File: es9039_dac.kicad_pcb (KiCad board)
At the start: 2 copper layers, 68.5 x 67.4 mm, 24 parts, among them J1 Conn_02x07_Odd_Even, U1 ES9039Q2M, U2 TPS7A2033DBV, U3 TPS7A2033DBV

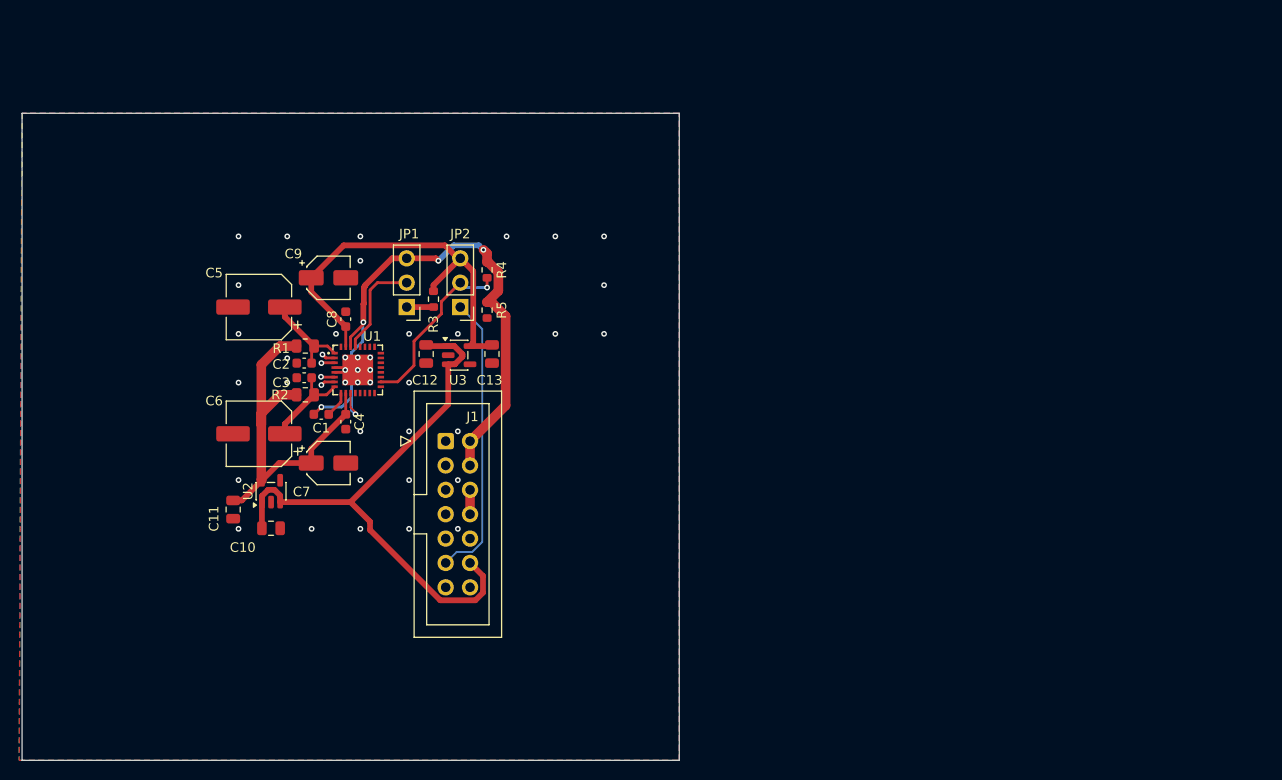
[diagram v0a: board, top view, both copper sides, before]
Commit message: deleted pcb and some changes in schematic
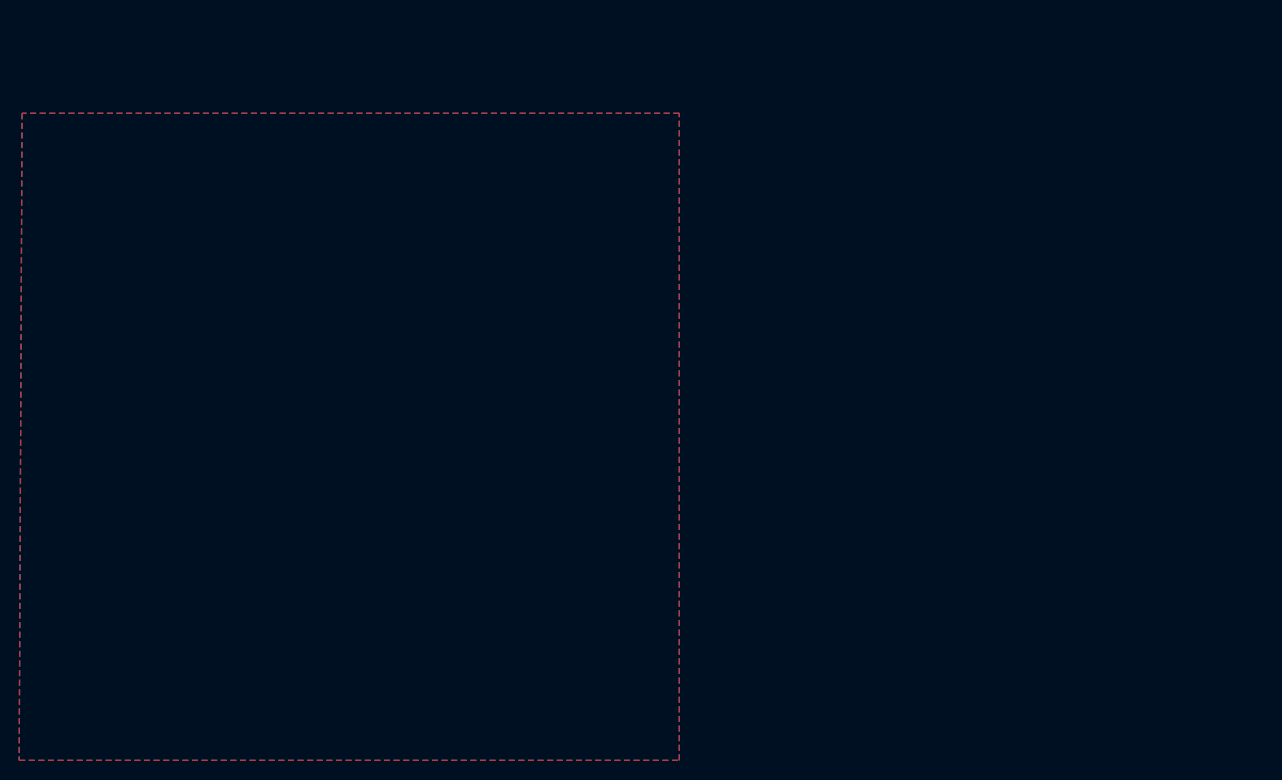
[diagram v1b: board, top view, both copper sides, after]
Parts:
- removed C1, C2, C3, C4, C8: 100n, Capacitor_SMD:C_0603_1608Metric
- removed C10, C11, C12, C13: 4u7, Capacitor_SMD:C_0805_2012Metric
- removed C5, C6: 100u, Capacitor_SMD:CP_Elec_6.3x5.8
- removed C7, C9: 10u, Capacitor_SMD:CP_Elec_4x5.4
- removed J1: Conn_02x07_Odd_Even, Connector_IDC:IDC-Header_2x07_P2.54mm_Vertical
- removed JP1: DAC_MODE1, Connector_PinHeader_2.54mm:PinHeader_1x03_P2.54mm_Vertical
- removed JP2: DAC_MODE2, Connector_PinHeader_2.54mm:PinHeader_1x03_P2.54mm_Vertical
- removed R1, R2: 2.2R, Resistor_SMD:R_0805_2012Metric
- removed R3: 10K, Resistor_SMD:R_0603_1608Metric
- removed R4: 100K, Resistor_SMD:R_0603_1608Metric
- removed R5: 0, Resistor_SMD:R_0603_1608Metric
- removed U1: ES9039Q2M, EasyEDA:QFN-32_L5.0-W5.0-P0.50-TL-EP3.2
- removed U2, U3: TPS7A2033DBV, Package_TO_SOT_SMD:SOT-23-5
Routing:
- net GNDD: track 65.2 -> 0.00 mm, vias 5 -> 0
- net +5V: track 61.2 -> 0.00 mm
- net +3.3V: track 42.7 -> 0.00 mm
- net +3.3VA: track 40.7 -> 0.00 mm
- net /STBY: track 30.4 -> 0.00 mm
- net Net-(JP2-C): track 18.8 -> 0.00 mm, vias 1 -> 0
- net /MODE: track 10.7 -> 0.00 mm
- net Net-(U1-AVCC_DAC2): track 9.70 -> 0.00 mm
- net Net-(U1-AVCC_DAC1): track 9.66 -> 0.00 mm
- net GNDA: track 7.57 -> 0.00 mm, vias 40 -> 0
- net Net-(JP1-A): track 2.79 -> 0.00 mm
- net Net-(U1-DVDD): track 2.74 -> 0.00 mm
- net unconnected-(U1-DAC2-Pad7): track 1.51 -> 0.00 mm, vias 1 -> 0
- net unconnected-(U1-DAC2B-Pad6): track 1.44 -> 0.00 mm, vias 1 -> 0
- net unconnected-(U1-DAC1B-Pad2): track 1.41 -> 0.00 mm, vias 1 -> 0
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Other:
- board outline removed
- copper layers 2 -> 4

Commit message: trace dac chip and add output stage
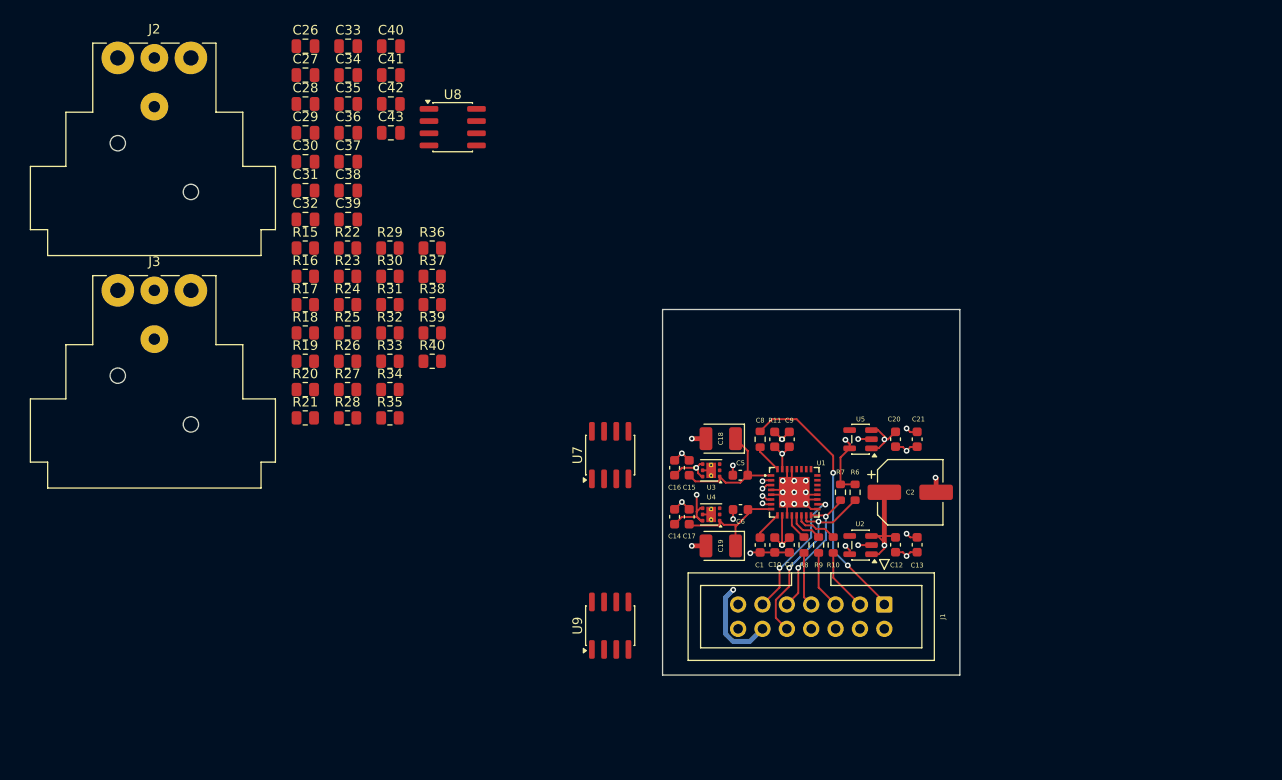
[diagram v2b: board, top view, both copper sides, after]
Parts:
- added C1: 100n, Capacitor_SMD:C_0603_1608Metric, F.Cu at (216.9, 100.7)
- added C10: 10u, Capacitor_SMD:C_0603_1608Metric, F.Cu at (218.4, 100.7)
- added C12: 4u7, Capacitor_SMD:C_0603_1608Metric, F.Cu at (231.0, 100.7)
- added C13: 4u7, Capacitor_SMD:C_0603_1608Metric, F.Cu at (233.3, 100.7)
- added C14: 1u, Capacitor_SMD:C_0603_1608Metric, F.Cu at (208.0, 97.8)
- added C15: 1u, Capacitor_SMD:C_0603_1608Metric, F.Cu at (209.5, 92.7)
- added C16: 1u, Capacitor_SMD:C_0603_1608Metric, F.Cu at (208.0, 92.7)
- added C17: 1u, Capacitor_SMD:C_0603_1608Metric, F.Cu at (209.5, 97.8)
- added C18: 47u, Capacitor_Tantalum_SMD:CP_EIA-3528-12_Kemet-T, F.Cu at (212.8, 89.7)
- added C19: 47u, Capacitor_Tantalum_SMD:CP_EIA-3528-12_Kemet-T, F.Cu at (212.8, 100.8)
- added C2: 100u, Capacitor_SMD:CP_Elec_6.3x5.8, F.Cu at (232.6, 95.2)
- added C20: 4u7, Capacitor_SMD:C_0603_1608Metric, F.Cu at (231.0, 89.7)
- added C21: 4u7, Capacitor_SMD:C_0603_1608Metric, F.Cu at (233.3, 89.7)
- added C26: 510p, Capacitor_SMD:C_0805_2012Metric, F.Cu at (169.5, 48.8)
- added C27: 510p, Capacitor_SMD:C_0805_2012Metric, F.Cu at (169.5, 51.8)
- added C28: 51p, Capacitor_SMD:C_0805_2012Metric, F.Cu at (169.5, 54.8)
- added C29: 2n2, Capacitor_SMD:C_0805_2012Metric, F.Cu at (169.5, 57.8)
- added C30: 2n2, Capacitor_SMD:C_0805_2012Metric, F.Cu at (169.5, 60.8)
- added C31: 470n, Capacitor_SMD:C_0805_2012Metric, F.Cu at (169.5, 63.8)
- added C32: 470n, Capacitor_SMD:C_0805_2012Metric, F.Cu at (169.5, 66.8)
- added C33: 2n2, Capacitor_SMD:C_0805_2012Metric, F.Cu at (174.0, 48.8)
- added C34: 2n2, Capacitor_SMD:C_0805_2012Metric, F.Cu at (174.0, 51.8)
- added C35: 510p, Capacitor_SMD:C_0805_2012Metric, F.Cu at (174.0, 54.8)
- added C36: 510p, Capacitor_SMD:C_0805_2012Metric, F.Cu at (174.0, 57.8)
- added C37: 51p, Capacitor_SMD:C_0805_2012Metric, F.Cu at (174.0, 60.8)
- added C38: 2n2, Capacitor_SMD:C_0805_2012Metric, F.Cu at (174.0, 63.8)
- added C39: 2n2, Capacitor_SMD:C_0805_2012Metric, F.Cu at (174.0, 66.8)
- added C4: 100n, Capacitor_SMD:C_0603_1608Metric, F.Cu at (220.0, 100.7)
- added C40: 470n, Capacitor_SMD:C_0805_2012Metric, F.Cu at (178.4, 48.8)
- added C41: 470n, Capacitor_SMD:C_0805_2012Metric, F.Cu at (178.4, 51.8)
- added C42: 470n, Capacitor_SMD:C_0805_2012Metric, F.Cu at (178.4, 54.8)
- added C43: 470n, Capacitor_SMD:C_0805_2012Metric, F.Cu at (178.4, 57.8)
- added C5: 100n, Capacitor_SMD:C_0603_1608Metric, F.Cu at (214.9, 93.5)
- added C6: 100n, Capacitor_SMD:C_0603_1608Metric, F.Cu at (214.9, 97.1)
- added C8: 100n, Capacitor_SMD:C_0603_1608Metric, F.Cu at (218.4, 89.7)
- added C9: 4u7, Capacitor_SMD:C_0603_1608Metric, F.Cu at (220.0, 89.7)
- added J1: Conn_02x07_Odd_Even, Connector_IDC:IDC-Header_2x07_P2.54mm_Vertical, F.Cu at (229.9, 106.9)
- added J2: XLR3, Connector_Audio:Jack_XLR_Neutrik_NC3MAH_Horizontal, F.Cu at (150.0, 50.0)
- added J3: XLR3, Connector_Audio:Jack_XLR_Neutrik_NC3MAH_Horizontal, F.Cu at (150.0, 74.2)
- added R10: 22R, Resistor_SMD:R_0603_1608Metric, F.Cu at (224.5, 100.7)
- added R11: 22R, Resistor_SMD:R_0603_1608Metric, F.Cu at (216.9, 89.7)
- added R15: 1K8, Resistor_SMD:R_0805_2012Metric, F.Cu at (169.5, 69.8)
- added R16: 1K8, Resistor_SMD:R_0805_2012Metric, F.Cu at (169.5, 72.7)
- added R17: 1K8, Resistor_SMD:R_0805_2012Metric, F.Cu at (169.5, 75.7)
- added R18: 1K8, Resistor_SMD:R_0805_2012Metric, F.Cu at (169.5, 78.6)
- added R19: 3K2, Resistor_SMD:R_0805_2012Metric, F.Cu at (169.5, 81.6)
- added R20: 3K2, Resistor_SMD:R_0805_2012Metric, F.Cu at (169.5, 84.5)
- added R21: 4R3, Resistor_SMD:R_0805_2012Metric, F.Cu at (169.5, 87.5)
- added R22: 4R3, Resistor_SMD:R_0805_2012Metric, F.Cu at (173.9, 69.8)
- added R23: 1M2, Resistor_SMD:R_0805_2012Metric, F.Cu at (173.9, 72.7)
- added R24: 10K, Resistor_SMD:R_0805_2012Metric, F.Cu at (173.9, 75.7)
- added R25: 10K, Resistor_SMD:R_0805_2012Metric, F.Cu at (173.9, 78.6)
- added R26: 140, Resistor_SMD:R_0805_2012Metric, F.Cu at (173.9, 81.6)
- added R27: 140, Resistor_SMD:R_0805_2012Metric, F.Cu at (173.9, 84.5)
- added R28: 4R3, Resistor_SMD:R_0805_2012Metric, F.Cu at (173.9, 87.5)
- added R29: 4R3, Resistor_SMD:R_0805_2012Metric, F.Cu at (178.3, 69.8)
- added R30: 1K8, Resistor_SMD:R_0805_2012Metric, F.Cu at (178.3, 72.7)
- added R31: 1K8, Resistor_SMD:R_0805_2012Metric, F.Cu at (178.3, 75.7)
- added R32: 1K8, Resistor_SMD:R_0805_2012Metric, F.Cu at (178.3, 78.6)
- added R33: 1K8, Resistor_SMD:R_0805_2012Metric, F.Cu at (178.3, 81.6)
- added R34: 3K2, Resistor_SMD:R_0805_2012Metric, F.Cu at (178.3, 84.5)
- added R35: 3K2, Resistor_SMD:R_0805_2012Metric, F.Cu at (178.3, 87.5)
- added R36: 1M2, Resistor_SMD:R_0805_2012Metric, F.Cu at (182.7, 69.8)
- added R37: 10K, Resistor_SMD:R_0805_2012Metric, F.Cu at (182.7, 72.7)
- added R38: 10K, Resistor_SMD:R_0805_2012Metric, F.Cu at (182.7, 75.7)
- added R39: 140, Resistor_SMD:R_0805_2012Metric, F.Cu at (182.7, 78.6)
- added R40: 140, Resistor_SMD:R_0805_2012Metric, F.Cu at (182.7, 81.6)
- added R6: 10K, Resistor_SMD:R_0603_1608Metric, F.Cu at (226.8, 95.2)
- added R7: 10K, Resistor_SMD:R_0603_1608Metric, F.Cu at (225.3, 95.2)
- added R8: 22R, Resistor_SMD:R_0603_1608Metric, F.Cu at (221.5, 100.7)
- added R9: 22R, Resistor_SMD:R_0603_1608Metric, F.Cu at (223.0, 100.7)
- added U1: ES9039Q2M, EasyEDA:QFN-32_L5.0-W5.0-P0.50-TL-EP3.2, F.Cu at (220.5, 95.2)
- added U2: TPS7A2033DBV, Package_TO_SOT_SMD:SOT-23-5, F.Cu at (227.4, 100.8)
- added U3: LP5912-3.3DRV, Package_SON:WSON-6-1EP_2x2mm_P0.65mm_EP1x1.6mm_ThermalVias, F.Cu at (211.8, 93.0)
- added U4: LP5912-3.3DRV, Package_SON:WSON-6-1EP_2x2mm_P0.65mm_EP1x1.6mm_ThermalVias, F.Cu at (211.8, 97.6)
- added U5: TPS7A2033DBV, Package_TO_SOT_SMD:SOT-23-5, F.Cu at (227.4, 89.7)
- added U7: OPA1612AxD, Package_SO:SOIC-8_3.9x4.9mm_P1.27mm, F.Cu at (201.3, 91.4)
- added U8: OPA1612AxD, Package_SO:SOIC-8_3.9x4.9mm_P1.27mm, F.Cu at (184.9, 57.2)
- added U9: OPA1612AxD, Package_SO:SOIC-8_3.9x4.9mm_P1.27mm, F.Cu at (201.3, 109.2)
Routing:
- net +5V: track 0.00 -> 81.9 mm, vias 0 -> 5
- net GNDA: track 0.00 -> 48.4 mm, vias 0 -> 22
- net /es9039_dac/I2S_MCLK: track 0.00 -> 27.4 mm, vias 0 -> 2
- net +3.3V: track 0.00 -> 25.9 mm, vias 0 -> 3
- net +3.3VA: track 0.00 -> 21.7 mm, vias 0 -> 3
- net /es9039_dac/I2C_SCL: track 0.00 -> 20.2 mm, vias 0 -> 2
- net /es9039_dac/I2C_SDA: track 0.00 -> 14.8 mm, vias 0 -> 2
- net /es9039_dac/DAC_STBY: track 0.00 -> 14.4 mm, vias 0 -> 2
- net +3.3VAL: track 0.00 -> 13.9 mm
- net +3.3VAR: track 0.00 -> 12.1 mm
- net /es9039_dac/I2S_DATA: track 0.00 -> 6.53 mm
- net /es9039_dac/I2S_LRCK: track 0.00 -> 6.12 mm
- net /es9039_dac/I2S_BCLK: track 0.00 -> 5.69 mm
- net Net-(U1-DATA2): track 0.00 -> 4.62 mm
- net Net-(U1-DATA1): track 0.00 -> 3.75 mm
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- added copper zone on In1.Cu, net GNDA
- removed copper zone on B.Cu, net GNDA
- removed copper zone on F.Cu, net GNDA
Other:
- board outline added: 31 x 38.1 mm

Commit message: traced o/s
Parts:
- added C44: 470n, Capacitor_SMD:C_0805_2012Metric, F.Cu at (263.9, 71.7)
- added C45: 470n, Capacitor_SMD:C_0805_2012Metric, F.Cu at (263.9, 74.7)
- added R1: 10K, Resistor_SMD:R_0805_2012Metric, F.Cu at (255.1, 65.1)
- added R12: 10K, Resistor_SMD:R_0805_2012Metric, F.Cu at (259.5, 65.1)
- added R13: 10K, Resistor_SMD:R_0805_2012Metric, F.Cu at (259.5, 68.1)
- added R14: 10K, Resistor_SMD:R_0805_2012Metric, F.Cu at (259.5, 71.0)
- added R2: 10K, Resistor_SMD:R_0805_2012Metric, F.Cu at (255.1, 68.1)
- added R3: 100R, Resistor_SMD:R_0805_2012Metric, F.Cu at (255.1, 71.0)
- added R4: 10K, Resistor_SMD:R_0805_2012Metric, F.Cu at (255.1, 74.0)
- added R41: 10K, Resistor_SMD:R_0805_2012Metric, F.Cu at (259.5, 74.0)
- added R42: 100R, Resistor_SMD:R_0805_2012Metric, F.Cu at (259.5, 76.9)
- added R5: 10K, Resistor_SMD:R_0805_2012Metric, F.Cu at (255.1, 76.9)
- added U6: OPA1612AxD, Package_SO:SOIC-8_3.9x4.9mm_P1.27mm, F.Cu at (265.9, 67.0)
- J2: value XLR3 -> XLR_L; footprint Connector_Audio:Jack_XLR_Neutrik_NC3MAH_Horizontal -> Connector_Audio:Jack_XLR_Neutrik_NC3MAH-0_Horizontal
- J3: value XLR3 -> XLR_R; footprint Connector_Audio:Jack_XLR_Neutrik_NC3MAH_Horizontal -> Connector_Audio:Jack_XLR_Neutrik_NC3MAH-0_Horizontal
- moved C34 64.7 mm to (208.3, 106.7), turned to 90 degrees
- moved J2 64.6 mm to (213.4, 62.2)
- moved C35 61.4 mm to (196.8, 111.8), turned to -90 degrees
- moved C31 59.2 mm to (199.4, 114.9), turned to 180 degrees
- moved C32 58.7 mm to (203.2, 114.9)
- moved C28 55.4 mm to (204.5, 97.8), turned to -90 degrees
- moved C36 54.0 mm to (196.8, 106.7), turned to 90 degrees
- moved C26 52.8 mm to (196.8, 94.0), turned to -90 degrees
- moved C33 52.8 mm to (208.3, 88.9), turned to 90 degrees
- moved C37 52.0 mm to (204.5, 102.9), turned to 90 degrees
- moved C38 49.0 mm to (184.2, 111.8), turned to -90 degrees
- moved C42 48.8 mm to (186.7, 102.9), turned to -90 degrees
- moved C27 46.1 mm to (196.8, 88.9), turned to 90 degrees
- moved R29 45.9 mm to (205.7, 106.7), turned to -90 degrees
- moved U8 43.7 mm to (191.8, 100.3), turned to -90 degrees
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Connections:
- net Net-(C29-Pad1) renamed OUT_L
- net Net-(C30-Pad1) renamed OUT_Lb
- net Net-(C38-Pad1) renamed OUT_R
- net Net-(C39-Pad1) renamed OUT_Rb
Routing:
- net +12V: track 0.00 -> 69.0 mm, vias 0 -> 8
- net -12V: track 0.00 -> 68.6 mm, vias 0 -> 7
- net OUT_R: track 0.00 -> 58.2 mm, vias 0 -> 1
- net OUT_Rb: track 0.00 -> 57.3 mm, vias 0 -> 1
- net OUT_Lb: track 0.00 -> 51.8 mm, vias 0 -> 1
- net OUT_L: track 0.00 -> 50.9 mm, vias 0 -> 1
- net DAC2: track 0.94 -> 37.3 mm, vias 1 -> 4
- net DAC2B: track 1.05 -> 36.3 mm, vias 1 -> 4
- net DAC1B: track 0.94 -> 31.9 mm, vias 1 -> 2
- net DAC1: track 1.05 -> 31.6 mm, vias 1 -> 4
- net Net-(C27-Pad2): track 0.00 -> 25.3 mm, vias 0 -> 2
- net Net-(C35-Pad2): track 0.00 -> 22.9 mm, vias 0 -> 2
- net Net-(C28-Pad1): track 0.00 -> 22.7 mm
- net Net-(C37-Pad1): track 0.00 -> 22.7 mm
- net Net-(U9B-+): track 0.00 -> 20.6 mm, vias 0 -> 2
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- added copper zone on In1.Cu, net (none)
- removed copper zone on In1.Cu, net GNDA
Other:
- board size 31 x 38.1 mm -> 65 x 68.6 mm

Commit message: add rca
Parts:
- added J4: RCA_R, rca:RCA-105A, F.Cu at (172.2, 60.7)
- added J5: XLR_L, Connector_Audio:Jack_XLR_Neutrik_NC3MAH-0_Horizontal, F.Cu at (234.9, 81.3)
- added J6: BAL_OUT, Connector_PinHeader_2.54mm:PinHeader_1x04_P2.54mm_Vertical, F.Cu at (213.5, 85.5)
- added J7: UNBAL_OUT, Connector_PinHeader_2.54mm:PinHeader_1x03_P2.54mm_Vertical, F.Cu at (175.3, 78.7)
- J2: value XLR_L -> RCA_L; footprint Connector_Audio:Jack_XLR_Neutrik_NC3MAH-0_Horizontal -> rca:RCA-105A
- U1: footprint EasyEDA:QFN-32_L5.0-W5.0-P0.50-TL-EP3.2 -> Package_DFN_QFN:QFN-32-1EP_5x5mm_P0.5mm_EP3.1x3.1mm_ThermalVias
- moved C44 95.6 mm to (173.4, 102.2), turned to -90 degrees
- moved C45 93.6 mm to (173.4, 98.4), turned to 90 degrees
- moved R14 93.2 mm to (173.4, 106.7), turned to -90 degrees
- moved U6 93.0 mm to (179.1, 100.3), turned to -90 degrees
- moved R13 92.1 mm to (175.9, 106.7), turned to 90 degrees
- moved R12 88.8 mm to (181.0, 106.7), turned to 90 degrees
- moved R41 87.4 mm to (178.4, 106.7), turned to 90 degrees
- moved R1 86.7 mm to (173.4, 94.0), turned to 90 degrees
- moved R42 81.9 mm to (178.4, 88.9), turned to 90 degrees
- moved R4 81.7 mm to (175.9, 94.0), turned to -90 degrees
- moved R2 80.9 mm to (178.4, 94.0), turned to -90 degrees
- moved R5 76.0 mm to (181.0, 94.0), turned to -90 degrees
- moved R3 75.6 mm to (181.6, 88.9), turned to 90 degrees
- moved J2 30.0 mm to (183.4, 60.7)
- moved J3 28.8 mm to (207.0, 81.3), turned to 180 degrees
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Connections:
- J2 pad 1: GNDA -> UNBAL_OUT_L
- J2 pad 2: OUT_Lb -> GNDA
- J2 pad 3: OUT_L -> (no net)
- J3 pad G: (no net) -> GNDA
- U6 pad 4: unconnected-(U6C-V--Pad4) -> -12V
- U6 pad 8: unconnected-(U6C-V+-Pad8) -> +12V
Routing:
- net OUT_Rb: track 57.3 -> 5.75 mm, vias 1 -> 0
- net OUT_R: track 58.2 -> 12.1 mm, vias 1 -> 0
- net OUT_Lb: track 51.8 -> 9.60 mm, vias 1 -> 3
- net OUT_L: track 50.9 -> 11.5 mm, vias 1 -> 0
- net +12V: track 69.0 -> 96.7 mm, vias 8 -> 9
- net Net-(R41-Pad2): track 0.00 -> 20.9 mm, vias 0 -> 2
- net -12V: track 68.6 -> 87.5 mm, vias 7 -> 8
- net Net-(R2-Pad2): track 0.00 -> 12.8 mm, vias 0 -> 2
- net Net-(U6A--): track 0.00 -> 9.98 mm
- net Net-(U6A-+): track 0.00 -> 6.55 mm
- net Net-(U6B-+): track 0.00 -> 6.03 mm
- net GNDA: track 64.0 -> 69.3 mm, vias 32 -> 26
- net Net-(U6B--): track 0.00 -> 3.30 mm
- added copper zone on In1.Cu, net GNDA
- removed copper zone on In1.Cu, net (none)
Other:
- board size 65 x 68.6 mm -> 80 x 55.9 mm

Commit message: almost ready
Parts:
- added G***: LOGO, logo:ess_logo_6mm, F.Cu at (216.0, 80.5)
- added REF**: KiCad-Logo2_6mm_SilkScreen, Symbol:KiCad-Logo2_6mm_SilkScreen, F.Cu at (183.0, 79.0)
- added REF**: MountingHole_3.2mm_M3, MountingHole:MountingHole_3.2mm_M3, F.Cu at (167.0, 88.0)
- added REF**: MountingHole_3.2mm_M3, MountingHole:MountingHole_3.2mm_M3, F.Cu at (241.0, 88.0)
- added REF**: MountingHole_3.2mm_M3, MountingHole:MountingHole_3.2mm_M3, F.Cu at (241.0, 111.5)
- added REF**: OSHW-Logo_5.7x6mm_SilkScreen, Symbol:OSHW-Logo_5.7x6mm_SilkScreen, F.Cu at (240.5, 99.5)
- added REF**: MountingHole_3.2mm_M3, MountingHole:MountingHole_3.2mm_M3, F.Cu at (167.0, 111.5)
- moved J6 48.7 mm to (168.5, 104.1), turned to 180 degrees
- moved J7 6.81 mm to (168.5, 79.5), turned to 180 degrees
- moved J4 1.96 mm to (170.2, 60.7)
- moved J5 1.30 mm to (233.7, 81.5)
- moved J2 1.14 mm to (182.2, 60.7)
- moved J3 1.03 mm to (206.0, 81.5)
- moved C43 0.73 mm to (186.5, 98.5)
- moved C42 0.65 mm to (186.5, 102.2)
- moved R12 0.53 mm to (181.5, 106.7)
- moved R14 0.53 mm to (173.9, 106.7)
- moved R41 0.53 mm to (179.0, 106.7)
- moved C44 0.53 mm to (173.9, 102.2)
- moved C45 0.53 mm to (173.9, 98.4)
- moved R1 0.53 mm to (173.9, 94.0)
- moved R2 0.53 mm to (179.0, 94.0)
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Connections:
- net /es9039_dac/DAC_STBY renamed /DAC_STBY
- net /es9039_dac/I2C_SCL renamed /I2C_SCL
- net /es9039_dac/I2C_SDA renamed /I2C_SDA
- net /es9039_dac/I2S_BCLK renamed /I2S_BCLK
- net /es9039_dac/I2S_DATA renamed /I2S_DATA
- net /es9039_dac/I2S_LRCK renamed /I2S_LRCK
- net /es9039_dac/I2S_MCLK renamed /I2S_MCLK
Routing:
- net OUT_Lb: track 9.60 -> 74.4 mm, vias 3 -> 6
- net OUT_L: track 11.5 -> 69.8 mm, vias 0 -> 1
- net OUT_R: track 12.1 -> 63.9 mm, vias 0 -> 1
- net OUT_Rb: track 5.75 -> 57.4 mm, vias 0 -> 3
- net UNBAL_OUT_L: track 0.00 -> 37.5 mm
- net UNBAL_OUT_R: track 0.00 -> 28.5 mm
- net Net-(U6B--): track 3.30 -> 8.71 mm
- net GNDA: track 69.3 -> 72.9 mm, vias 26 -> 25
- net +12V: track 96.7 -> 95.1 mm
- net -12V: track 87.5 -> 89.0 mm
- net Net-(U6A--): track 9.98 -> 9.14 mm
- net Net-(U6B-+): track 6.03 -> 5.19 mm
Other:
- board size 80 x 55.9 mm -> 82.2 x 55.9 mm
- board text added: "github.com/0xngd"
